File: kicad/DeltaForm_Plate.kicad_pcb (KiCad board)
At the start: 2 copper layers, 85.4 x 128.6 mm, 0 parts

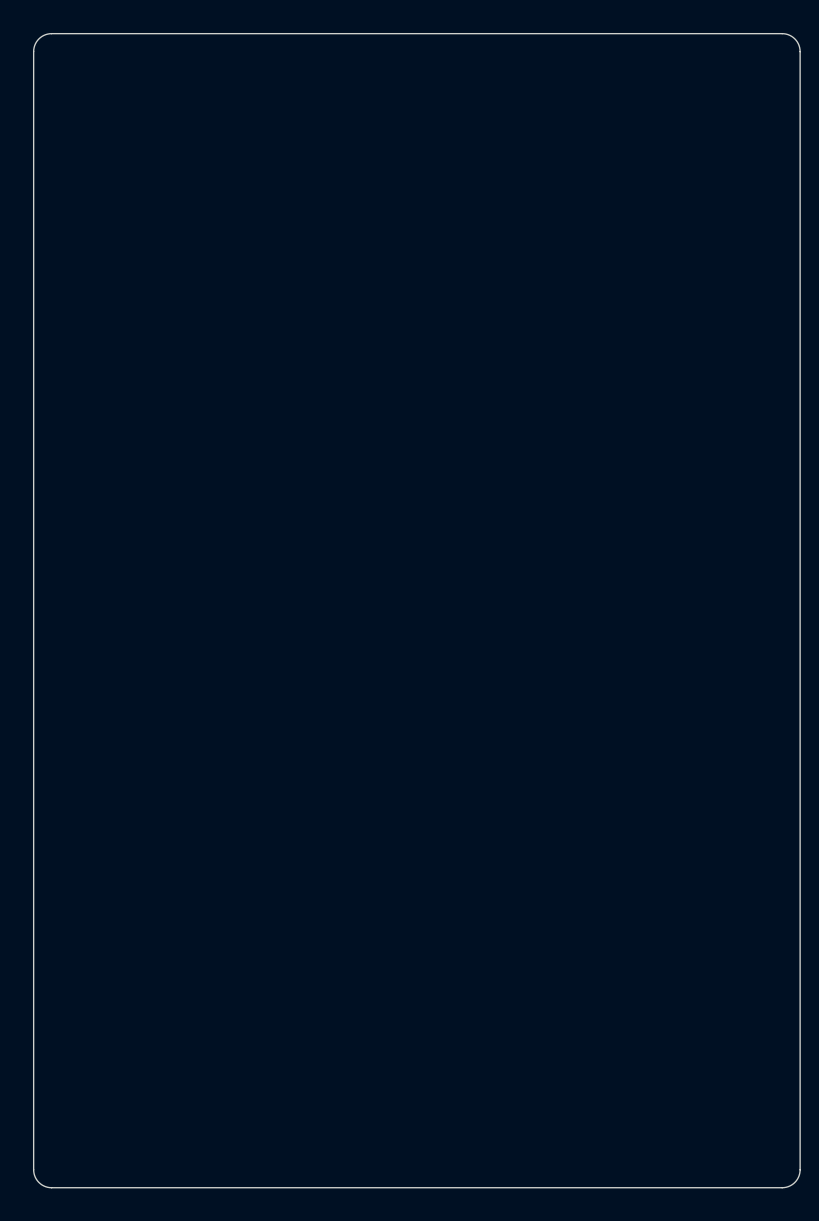
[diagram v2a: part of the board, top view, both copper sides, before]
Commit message: screw holes
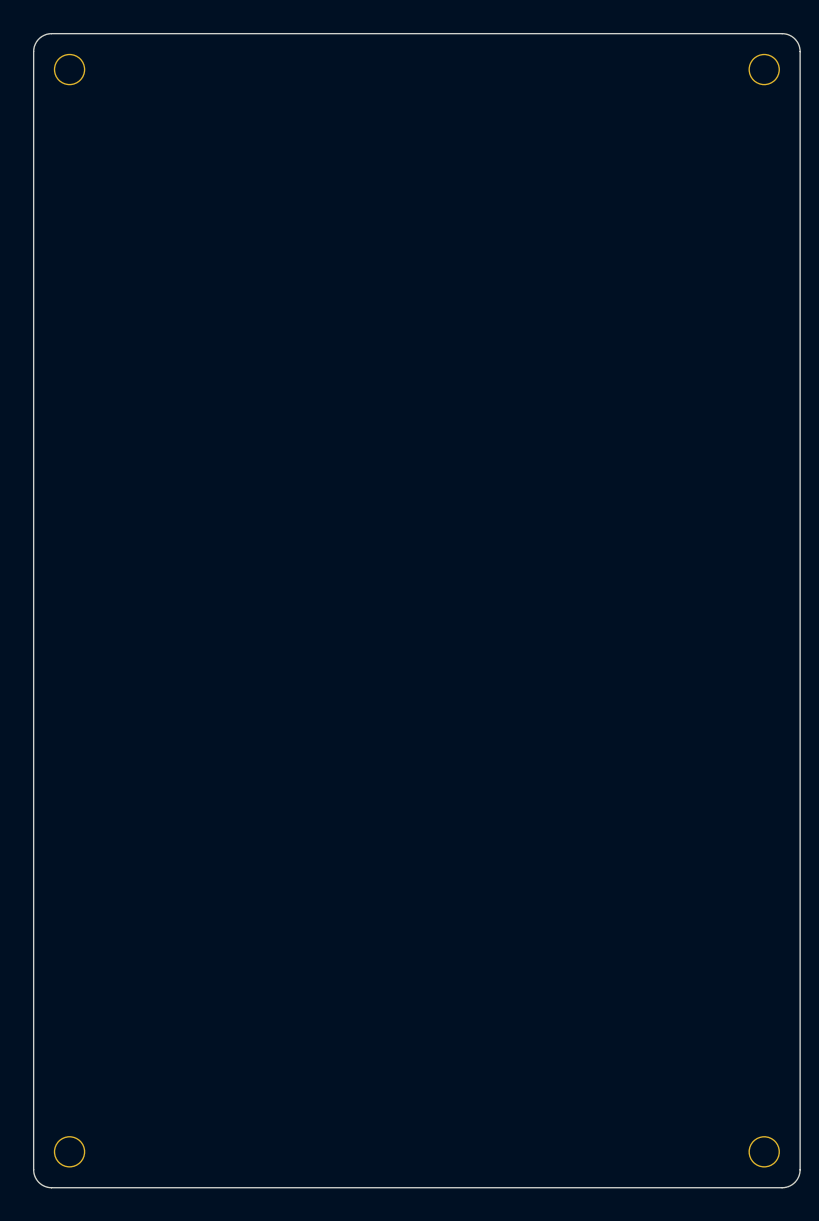
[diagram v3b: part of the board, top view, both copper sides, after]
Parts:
- added H1: MountingHole_3.2mm_Pad, TB2086_MISC:MountingHole_3.2mm_Pad, F.Cu at (437.2, 79.7)
- added H2: MountingHole_3.2mm_Pad, TB2086_MISC:MountingHole_3.2mm_Pad, F.Cu at (514.6, 79.7)
- added H3: MountingHole_3.2mm_Pad, TB2086_MISC:MountingHole_3.2mm_Pad, F.Cu at (514.6, 200.3)
- added H4: MountingHole_3.2mm_Pad, TB2086_MISC:MountingHole_3.2mm_Pad, F.Cu at (437.2, 200.3)
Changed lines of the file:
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@@
     (title "DeltaForm_Plate")
     (date "2025-07-03")
-    (rev "0.3.4")
+    (rev "0.3.5")
     (company "Allen Choi")
   )
@@
     )
   )
+(
+         footprint "TB2086_MISC:MountingHole_3.2mm_Pad"
+        (version 20241229)
+        (generator "pcbnew")
+        (generator_version "9.0")
+        (layer "F.Cu")
+        (descr "Mounting Hole 3.2mm, no annular, M3")
+        (tags "mounting hole 3.2mm no annular m3")
+        (property "Reference" "H1" (at 0 -4.2 0) (layer "F.SilkS") hide  (effects (font (size 1 1) (thickness 0.15))))
+        (attr exclude_from_pos_files exclude_from_bom)
+        (embedded_fonts no)
+        (at 437.17500000000007 79.7125 0)
+        (property "Value" "MountingHole_3.2mm_Pad" (at 0 4.2 0) (layer "F.Fab")  (effects (font (size 1 1) (thickness 0.15))))
+        (property "Datasheet" "" (at 0 0 0) (unlocked yes) (layer "F.Fab") (hide yes)  (effects (font (size 1.27 1.27) (thickness 0.15))))
+        (property "Description" "" (at 0 0 0) (unlocked yes) (layer "F.Fab") (hide yes)  (effects (font (size 1.27 1.27) (thickness 0.15))))
+        (fp_text user "${REFERENCE}" (at 0 0 0) (layer "F.Fab")  (effects (font (size 1 1) (thickness 0.15))))
+        (fp_circle (center 0 0) (end 3.45 0) (stroke (width 0.05) (type solid)) (fill no) (layer "F.CrtYd") )
+        (pad "1" thru_hole circle (at 0 0 0) (size 3.5 3.5) (drill 3.2) (layers "*.Cu" "*.Mask") (remove_unused_layers no) (zone_connect 2)  (net 1 "GND"))
+        (fp_circle (center 0 0) (end 3.2 0) (stroke (width 0.15) (type solid)) (fill no) (layer "Cmts.User") )
+            )
+(
+         footprint "TB2086_MISC:MountingHole_3.2mm_Pad"
+        (version 20241229)
+        (generator "pcbnew")
+        (generator_version "9.0")
+        (layer "F.Cu")
+        (descr "Mounting Hole 3.2mm, no annular, M3")
+        (tags "mounting hole 3.2mm no annular m3")
+        (property "Reference" "H2" (at 0 -4.2 0) (layer "F.SilkS") hide  (effects (font (size 1 1) (thickness 0.15))))
+        (attr exclude_from_pos_files exclude_from_bom)
+        (embedded_fonts no)
+        (at 514.575 79.7125 0)
+        (property "Value" "MountingHole_3.2mm_Pad" (at 0 4.2 0) (layer "F.Fab")  (effects (font (size 1 1) (thickness 0.15))))
+        (property "Datasheet" "" (at 0 0 0) (unlocked yes) (layer "F.Fab") (hide yes)  (effects (font (size 1.27 1.27) (thickness 0.15))))
+        (property "Description" "" (at 0 0 0) (unlocked yes) (layer "F.Fab") (hide yes)  (effects (font (size 1.27 1.27) (thickness 0.15))))
+        (fp_text user "${REFERENCE}" (at 0 0 0) (layer "F.Fab")  (effects (font (size 1 1) (thickness 0.15))))
+        (fp_circle (center 0 0) (end 3.45 0) (stroke (width 0.05) (type solid)) (fill no) (layer "F.CrtYd") )
+        (pad "1" thru_hole circle (at 0 0 0) (size 3.5 3.5) (drill 3.2) (layers "*.Cu" "*.Mask") (remove_unused_layers no) (zone_connect 2)  (net 1 "GND"))
+        (fp_circle (center 0 0) (end 3.2 0) (stroke (width 0.15) (type solid)) (fill no) (layer "Cmts.User") )
+            )
+(
+         footprint "TB2086_MISC:MountingHole_3.2mm_Pad"
+        (version 20241229)
+        (generator "pcbnew")
+        (generator_version "9.0")
+        (layer "F.Cu")
+        (descr "Mounting Hole 3.2mm, no annular, M3")
+        (tags "mounting hole 3.2mm no annular m3")
+        (property "Reference" "H3" (at 0 -4.2 0) (layer "F.SilkS") hide  (effects (font (size 1 1) (thickness 0.15))))
+        (attr exclude_from_pos_files exclude_from_bom)
+        (embedded_fonts no)
+        (at 514.575 200.30000000000004 0)
+        (property "Value" "MountingHole_3.2mm_Pad" (at 0 4.2 0) (layer "F.Fab")  (effects (font (size 1 1) (thickness 0.15))))
+        (property "Datasheet" "" (at 0 0 0) (unlocked yes) (layer "F.Fab") (hide yes)  (effects (font (size 1.27 1.27) (thickness 0.15))))
+        (property "Description" "" (at 0 0 0) (unlocked yes) (layer "F.Fab") (hide yes)  (effects (font (size 1.27 1.27) (thickness 0.15))))
+        (fp_text user "${REFERENCE}" (at 0 0 0) (layer "F.Fab")  (effects (font (size 1 1) (thickness 0.15))))
+        (fp_circle (center 0 0) (end 3.45 0) (stroke (width 0.05) (type solid)) (fill no) (layer "F.CrtYd") )
+        (pad "1" thru_hole circle (at 0 0 0) (size 3.5 3.5) (drill 3.2) (layers "*.Cu" "*.Mask") (remove_unused_layers no) (zone_connect 2)  (net 1 "GND"))
+        (fp_circle (center 0 0) (end 3.2 0) (stroke (width 0.15) (type solid)) (fill no) (layer "Cmts.User") )
+            )
+(
+         footprint "TB2086_MISC:MountingHole_3.2mm_Pad"
+        (version 20241229)
+        (generator "pcbnew")
+        (generator_version "9.0")
+        (layer "F.Cu")
+        (descr "Mounting Hole 3.2mm, no annular, M3")
+        (tags "mounting hole 3.2mm no annular m3")
+        (property "Reference" "H4" (at 0 -4.2 0) (layer "F.SilkS") hide  (effects (font (size 1 1) (thickness 0.15))))
+        (attr exclude_from_pos_files exclude_from_bom)
+        (embedded_fonts no)
+        (at 437.17500000000007 200.30000000000004 0)
+        (property "Value" "MountingHole_3.2mm_Pad" (at 0 4.2 0) (layer "F.Fab")  (effects (font (size 1 1) (thickness 0.15))))
+        (property "Datasheet" "" (at 0 0 0) (unlocked yes) (layer "F.Fab") (hide yes)  (effects (font (size 1.27 1.27) (thickness 0.15))))
+        (property "Description" "" (at 0 0 0) (unlocked yes) (layer "F.Fab") (hide yes)  (effects (font (size 1.27 1.27) (thickness 0.15))))
+        (fp_text user "${REFERENCE}" (at 0 0 0) (layer "F.Fab")  (effects (font (size 1 1) (thickness 0.15))))
+        (fp_circle (center 0 0) (end 3.45 0) (stroke (width 0.05) (type solid)) (fill no) (layer "F.CrtYd") )
+        (pad "1" thru_hole circle (at 0 0 0) (size 3.5 3.5) (drill 3.2) (layers "*.Cu" "*.Mask") (remove_unused_layers no) (zone_connect 2)  (net 1 "GND"))
+        (fp_circle (center 0 0) (end 3.2 0) (stroke (width 0.15) (type solid)) (fill no) (layer "Cmts.User") )
+            )
   (gr_line (start 433.17500000000007 202.3) (end 433.17500000000007 77.7125) (layer Edge.Cuts) (stroke (width 0.15) (type default)))
 (gr_line (start 435.17500000000007 75.7125) (end 516.575 75.7125) (layer Edge.Cuts) (stroke (width 0.15) (type default)))

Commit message: pogo pin - ergogen
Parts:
- moved H1 270.0 mm to (167.2, 79.7)
- moved H2 270.0 mm to (244.6, 79.7)
- moved H3 270.0 mm to (244.6, 200.3)
- moved H4 270.0 mm to (167.2, 200.3)

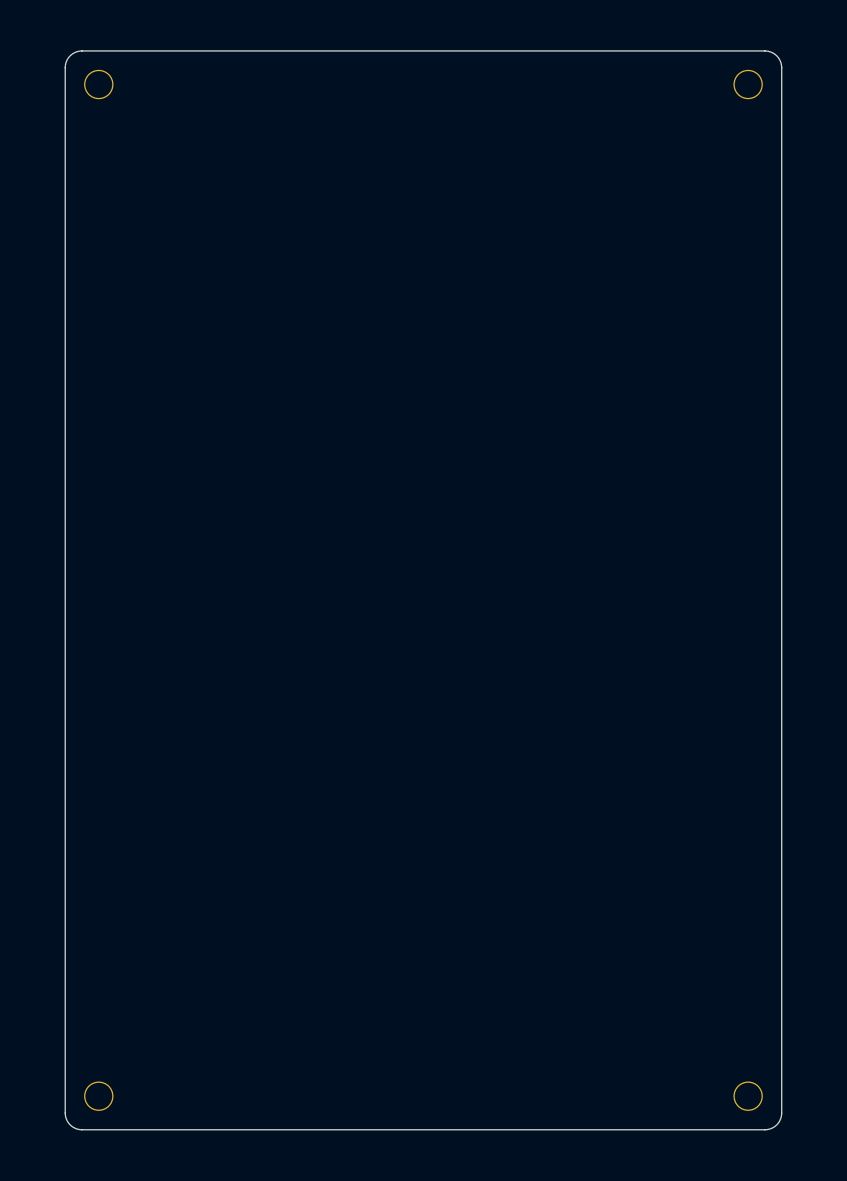
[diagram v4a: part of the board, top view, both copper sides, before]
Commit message: changed screw sizes
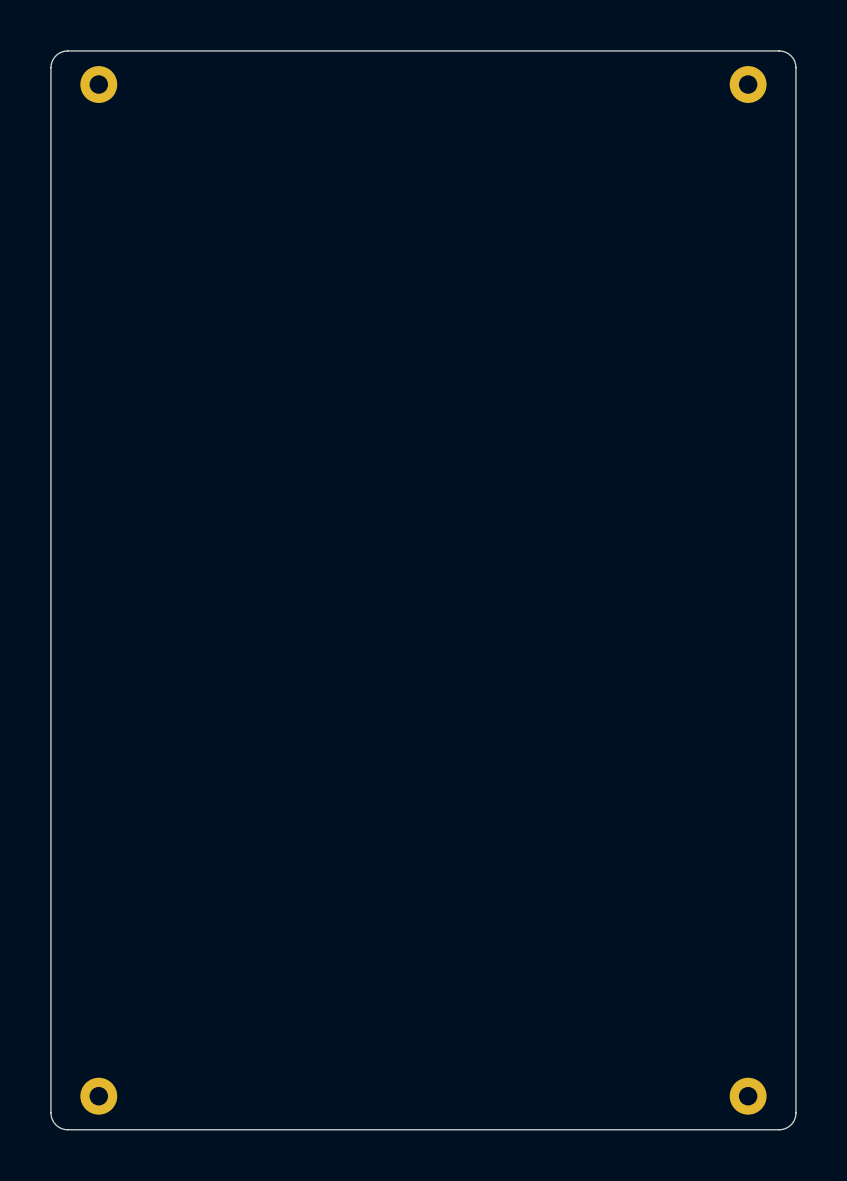
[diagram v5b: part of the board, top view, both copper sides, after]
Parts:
- H1, H2, H3, H4: value MountingHole_3.2mm_Pad -> MountingHole_2.2mm_M2_Pad; footprint TB2086_MISC:MountingHole_3.2mm_Pad -> TB2086_MISC:MountingHole_2.2mm_M2_Pad
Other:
- board size 85.4 x 128.6 mm -> 88.8 x 128.6 mm
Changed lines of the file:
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@@
 	(title_block
 		(title "DeltaForm_Plate")
-		(date "2025-07-04")
-		(rev "0.3.6")
+		(date "2025-07-08")
+		(rev "0.4.3")
 		(company "Allen Choi")
 	)
@@
 	(net 0 "")
 	(net 1 "GND")
-	(footprint "TB2086_MISC:MountingHole_3.2mm_Pad"
+	(footprint "TB2086_MISC:MountingHole_2.2mm_M2_Pad"
 		(layer "F.Cu")
-		(at 244.575 79.7125)
-		(descr "Mounting Hole 3.2mm, no annular, M3")
-		(tags "mounting hole 3.2mm no annular m3")
-		(property "Reference" "H2"
-			(at 0 -4.2 0)
+		(at 167.175 200.3)
+		(descr "Mounting Hole 2.2mm, M2")
+		(tags "mounting hole 2.2mm m2")
+		(property "Reference" "H4"
+			(at 0 -3.2 0)
 			(layer "F.SilkS")
 			(hide yes)
@@
 			)
 		)
-		(property "Value" "MountingHole_3.2mm_Pad"
-			(at 0 4.2 0)
+		(property "Value" "MountingHole_2.2mm_M2_Pad"
+			(at 0 3.2 0)
 			(layer "F.Fab")
 			(effects
@@
 		(fp_circle
 			(center 0 0)
-			(end 3.2 0)
+			(end 2.2 0)
 			(stroke
 				(width 0.15)
@@
 		(fp_circle
 			(center 0 0)
-			(end 3.45 0)
+			(end 2.45 0)
 			(stroke
 				(width 0.05)
@@
 		(pad "1" thru_hole circle
 			(at 0 0)
-			(size 3.5 3.5)
-			(drill 3.2)
+			(size 4.4 4.4)
+			(drill 2.2)
 			(layers "*.Cu" "*.Mask")
 			(remove_unused_layers no)
 			(net 1 "GND")
-			(zone_connect 2)
 		)
 		(embedded_fonts no)
 	)
-	(footprint "TB2086_MISC:MountingHole_3.2mm_Pad"
+	(footprint "TB2086_MISC:MountingHole_2.2mm_M2_Pad"
 		(layer "F.Cu")
-		(at 167.175 79.7125)
-		(descr "Mounting Hole 3.2mm, no annular, M3")
-		(tags "mounting hole 3.2mm no annular m3")
-		(property "Reference" "H1"
-			(at 0 -4.2 0)
+		(at 244.575 200.3)
+		(descr "Mounting Hole 2.2mm, M2")
+		(tags "mounting hole 2.2mm m2")
+		(property "Reference" "H3"
+			(at 0 -3.2 0)
 			(layer "F.SilkS")
 			(hide yes)
@@
 			)
 		)
-		(property "Value" "MountingHole_3.2mm_Pad"
-			(at 0 4.2 0)
+		(property "Value" "MountingHole_2.2mm_M2_Pad"
+			(at 0 3.2 0)
 			(layer "F.Fab")
 			(effects
@@
 		(fp_circle
 			(center 0 0)
-			(end 3.2 0)
+			(end 2.2 0)
 			(stroke
 				(width 0.15)
@@
 		(fp_circle
 			(center 0 0)
-			(end 3.45 0)
+			(end 2.45 0)
 			(stroke
 				(width 0.05)
@@
 		(pad "1" thru_hole circle
 			(at 0 0)
-			(size 3.5 3.5)
-			(drill 3.2)
+			(size 4.4 4.4)
+			(drill 2.2)
 			(layers "*.Cu" "*.Mask")
 			(remove_unused_layers no)
 			(net 1 "GND")
-			(zone_connect 2)
 		)
 		(embedded_fonts no)
 	)
-	(footprint "TB2086_MISC:MountingHole_3.2mm_Pad"
+	(footprint "TB2086_MISC:MountingHole_2.2mm_M2_Pad"
 		(layer "F.Cu")
-		(at 167.175 200.3)
-		(descr "Mounting Hole 3.2mm, no annular, M3")
-		(tags "mounting hole 3.2mm no annular m3")
-		(property "Reference" "H4"
-			(at 0 -4.2 0)
+		(at 244.575 79.7125)
+		(descr "Mounting Hole 2.2mm, M2")
+		(tags "mounting hole 2.2mm m2")
+		(property "Reference" "H2"
+			(at 0 -3.2 0)
 			(layer "F.SilkS")
 			(hide yes)
@@
 			)
 		)
-		(property "Value" "MountingHole_3.2mm_Pad"
-			(at 0 4.2 0)
+		(property "Value" "MountingHole_2.2mm_M2_Pad"
+			(at 0 3.2 0)
 			(layer "F.Fab")
 			(effects
@@
 		(fp_circle
 			(center 0 0)
-			(end 3.2 0)
+			(end 2.2 0)
 			(stroke
 				(width 0.15)
@@
 		(fp_circle
 			(center 0 0)
-			(end 3.45 0)
+			(end 2.45 0)
 			(stroke
 				(width 0.05)
@@
 		(pad "1" thru_hole circle
 			(at 0 0)
-			(size 3.5 3.5)
-			(drill 3.2)
+			(size 4.4 4.4)
+			(drill 2.2)
 			(layers "*.Cu" "*.Mask")
 			(remove_unused_layers no)
 			(net 1 "GND")
-			(zone_connect 2)
 		)
 		(embedded_fonts no)
 	)
-	(footprint "TB2086_MISC:MountingHole_3.2mm_Pad"
+	(footprint "TB2086_MISC:MountingHole_2.2mm_M2_Pad"
 		(layer "F.Cu")
-		(at 244.575 200.3)
-		(descr "Mounting Hole 3.2mm, no annular, M3")
-		(tags "mounting hole 3.2mm no annular m3")
-		(property "Reference" "H3"
-			(at 0 -4.2 0)
+		(at 167.175 79.7125)
+		(descr "Mounting Hole 2.2mm, M2")
+		(tags "mounting hole 2.2mm m2")
+		(property "Reference" "H1"
+			(at 0 -3.2 0)
 			(layer "F.SilkS")
 			(hide yes)
@@
 			)
 		)
-		(property "Value" "MountingHole_3.2mm_Pad"
-			(at 0 4.2 0)
+		(property "Value" "MountingHole_2.2mm_M2_Pad"
+			(at 0 3.2 0)
 			(layer "F.Fab")
 			(effects
@@
 		(fp_circle
 			(center 0 0)
-			(end 3.2 0)
+			(end 2.2 0)
 			(stroke
 				(width 0.15)
@@
 		(fp_circle
 			(center 0 0)
-			(end 3.45 0)
+			(end 2.45 0)
 			(stroke
 				(width 0.05)
@@
 		(pad "1" thru_hole circle
 			(at 0 0)
-			(size 3.5 3.5)
-			(drill 3.2)
+			(size 4.4 4.4)
+			(drill 2.2)
 			(layers "*.Cu" "*.Mask")
 			(remove_unused_layers no)
 			(net 1 "GND")
-			(zone_connect 2)
 		)
 		(embedded_fonts no)
 	)
 	(gr_line
-		(start 246.575 204.3)
-		(end 165.175 204.3)
+		(start 163.475 75.7125)
+		(end 248.275 75.7125)
+		(stroke
+			(width 0.15)
+			(type default)
+		)
+		(layer "Edge.Cuts")
+	)
+	(gr_line
+		(start 250.275 77.7125)
+		(end 250.275 202.3)
+		(stroke
+			(width 0.15)
+			(type default)
+		)
+		(layer "Edge.Cuts")
+	)
+	(gr_line
+		(start 161.475 202.3)
+		(end 161.475 77.7125)
 		(stroke
 			(width 0.15)
@@
 	)
 	(gr_arc
-		(start 246.575 75.7125)
-		(mid 247.989214 76.298286)
-		(end 248.575 77.7125)
+		(start 163.475 204.3)
+		(mid 162.060786 203.714214)
+		(end 161.475 202.3)
 		(stroke
 			(width 0.15)
@@
 	)
 	(gr_arc
-		(start 163.175 77.7125)
-		(mid 163.760786 76.298286)
-		(end 165.175 75.7125)
+		(start 161.475 77.7125)
+		(mid 162.060786 76.298286)
+		(end 163.475 75.7125)
 		(stroke
 			(width 0.15)
@@
 	)
 	(gr_line
-		(start 165.175 75.7125)
-		(end 246.575 75.7125)
-		(stroke
-			(width 0.15)
-			(type default)
-		)
-		(layer "Edge.Cuts")
-	)
-	(gr_line
-		(start 163.175 202.3)
-		(end 163.175 77.7125)
+		(start 248.275 204.3)
+		(end 163.475 204.3)
 		(stroke
 			(width 0.15)
@@
 	)
 	(gr_arc
-		(start 165.175 204.3)
-		(mid 163.760786 203.714214)
-		(end 163.175 202.3)
-		(stroke
-			(width 0.15)
-			(type default)
-		)
-		(layer "Edge.Cuts")
-	)
-	(gr_line
-		(start 248.575 77.7125)
-		(end 248.575 202.3)
+		(start 248.275 75.7125)
+		(mid 249.689214 76.298286)
+		(end 250.275 77.7125)
 		(stroke
 			(width 0.15)
@@
 	)
 	(gr_arc
-		(start 248.575 202.3)
-		(mid 247.989214 203.714214)
-		(end 246.575 204.3)
-		(stroke
-			(width 0.15)
+		(start 250.275 202.3)
+		(mid 249.689214 203.714214)
+		(end 248.275 204.3)
+		(stroke
+			(width 0.15)

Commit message: fixed positions for screw holes
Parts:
- moved H1 271.0 mm to (438.2, 80.7)
- moved H4 271.0 mm to (438.2, 199.3)
- moved H2 269.0 mm to (513.6, 80.7)
- moved H3 269.0 mm to (513.6, 199.3)

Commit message: more tweaks  (#3)
* small tweaks

* GlyphMatrix - 3mm screws

* PhaseShift - 3mm screws

* DeltaForm - 3mm screws

* updated README.md
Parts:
- H1, H2, H3, H4: value MountingHole_2.2mm_M2_Pad -> MountingHole_3.2mm_Pad; footprint TB2086_MISC:MountingHole_2.2mm_M2_Pad -> TB2086_MISC:MountingHole_3.2mm_Pad
- moved H1 270.5 mm to (167.7, 80.2)
- moved H4 270.5 mm to (167.7, 199.8)
- moved H2 269.5 mm to (244.1, 80.2)
- moved H3 269.5 mm to (244.1, 199.8)

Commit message: plates (#4)
* Silk Screen

* small changes for GlyphMatrix

* Silk screen for plates

* amended GlyphMatrix
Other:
- board text added: "DeltaForm"
